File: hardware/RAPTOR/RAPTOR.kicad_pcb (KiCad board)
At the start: 2 copper layers, 101.6 x 55.9 mm, 49 parts, among them J1 SOLC_CONN, J10 EXT_LED3, J11 SRVOL_CONN, J12 SRVOR_CONN, J13 HOTWIRE_CONN, J14 RBF_CONN, J15 EEPROM_BTN_CONN, J16 SOLC_SW_CONN, J17 SOLP_SW_CONN, J18 CONN_BUZZER, J2 SOLP_CONN, J3 JST_2MM_MALE, J4 CONN_LED_FIX, J5 CONN_SOLP_LED, J6 CONN_SOLC_LED, J7 EXT_LED0, J8 EXT_LED1, J9 EXT_LED2, P1 Power, P2 Analog, P3 Digital, P4 Digital, P5 CONN_01X01, P6 CONN_01X01, P7 CONN_01X01, P8 CONN_01X01, Q1 MOSFET-NCH-STQ2NK60ZR-AP, Q2 MOSFET-NCH-STQ2NK60ZR-AP, Q3 MOSFET-NCH-STQ2NK60ZR-AP, Q4 MOSFET-NCH-STQ2NK60ZR-AP, Q5 MOSFET-NCH-STQ2NK60ZR-AP, SW1 SW_Push_Open, SW2 SW_Push_Open, U1 BMP280 Breakout, U2 BNO055 Breakout, U3 OpenLog, U4 AdafruitGPS, U5 U3V12F12, U6 D24V550F5

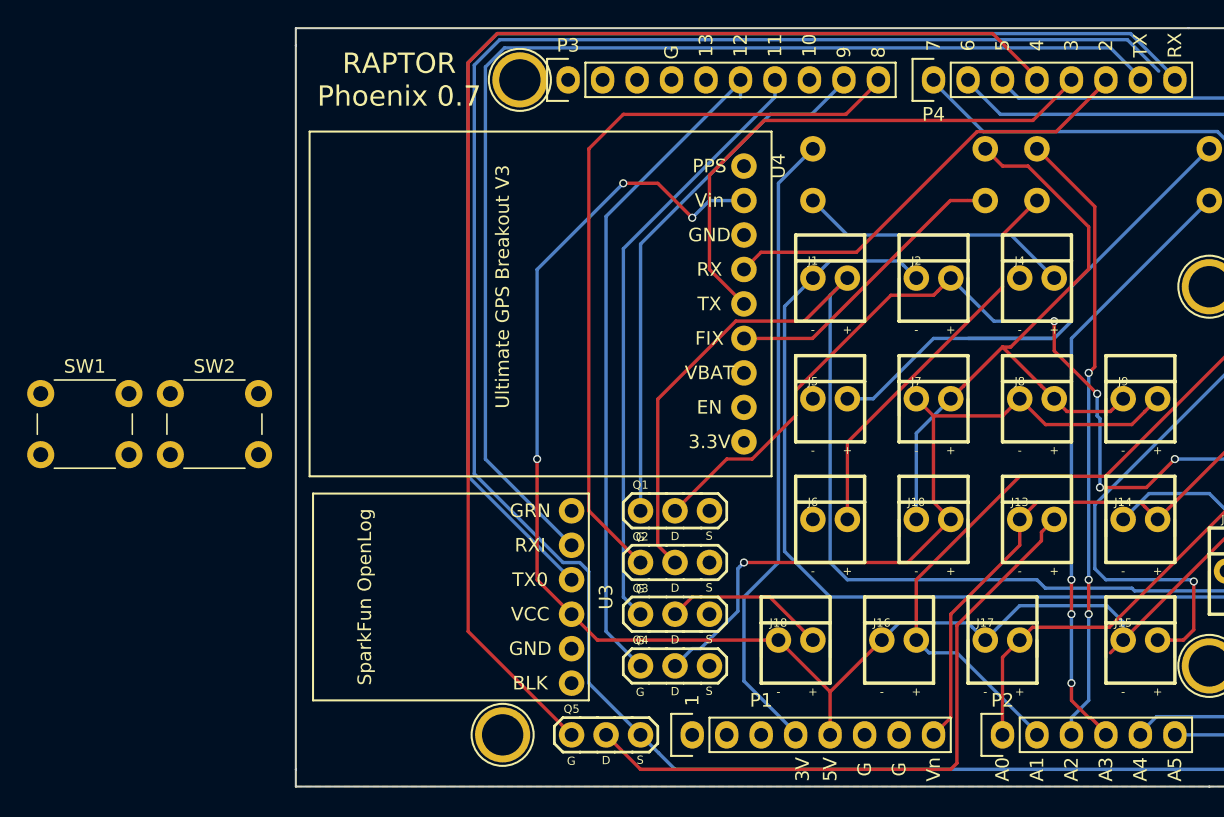
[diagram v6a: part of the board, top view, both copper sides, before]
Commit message: Finished Roouting
Needs checking though. Full error and netlist tests
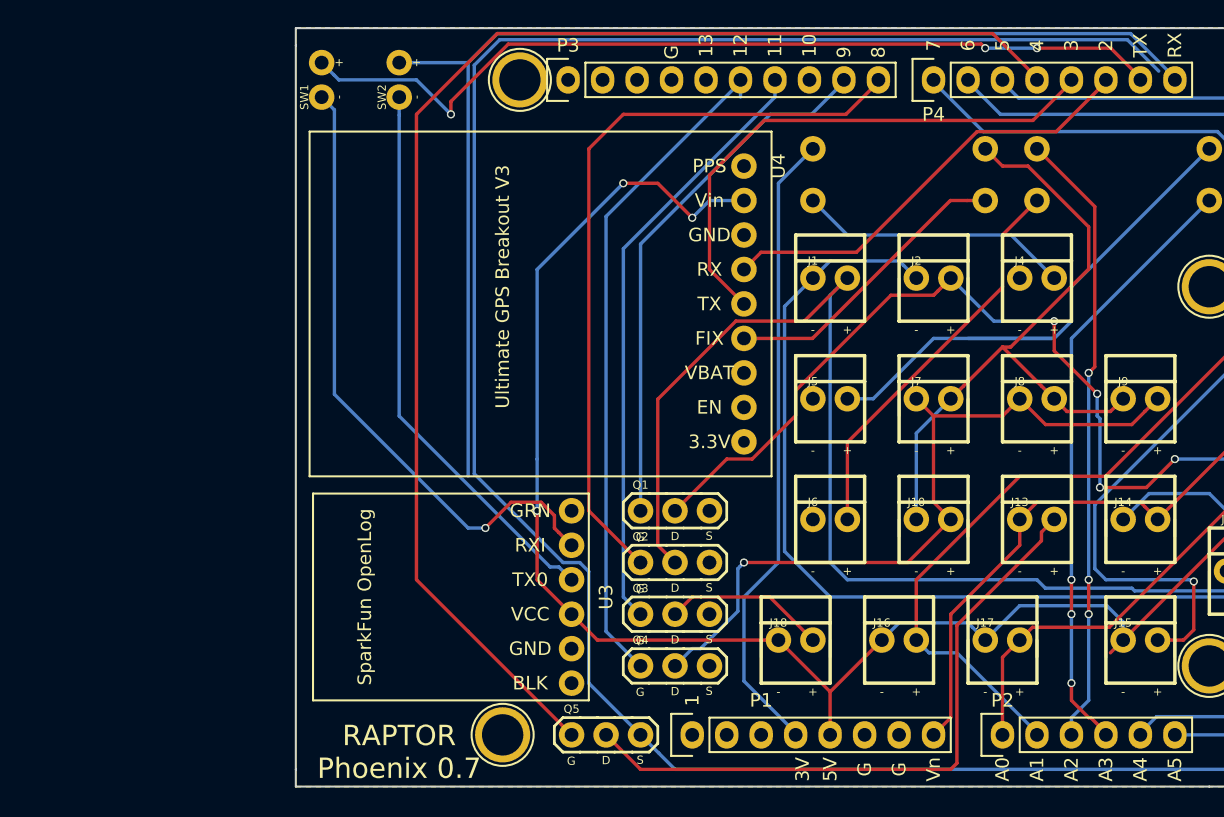
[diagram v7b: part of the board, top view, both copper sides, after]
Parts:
- SW1, SW2: footprint Button_Switch_THT:SW_PUSH_6mm -> RAPTOR_footprints:Jumper
- moved SW1 30.5 mm to (112.3, 76.8), turned to 90 degrees
- moved SW2 28.0 mm to (118.0, 76.8), turned to 90 degrees
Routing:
- net Net-(SW1-Pad1): track 0.00 -> 46.5 mm, vias 0 -> 1
- net Net-(SW2-Pad1): track 0.00 -> 41.2 mm
- net /SD_RX: track 87.8 -> 65.9 mm, vias 0 -> 3
- net /SD_TX: track 95.7 -> 90.0 mm
- net /HOTWIRE: track 97.0 -> 100.1 mm
